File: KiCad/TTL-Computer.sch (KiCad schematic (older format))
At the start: 0 parts

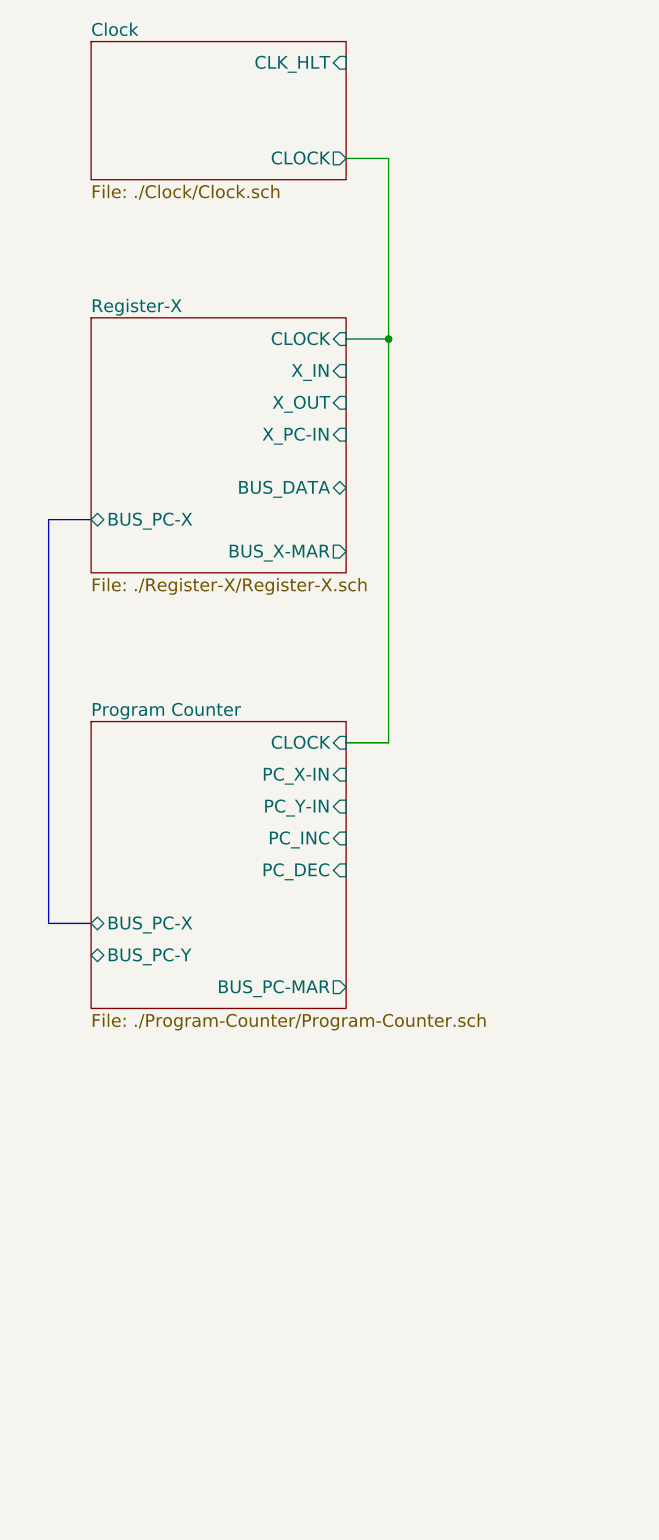
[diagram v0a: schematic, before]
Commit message: Started work on Program Counter
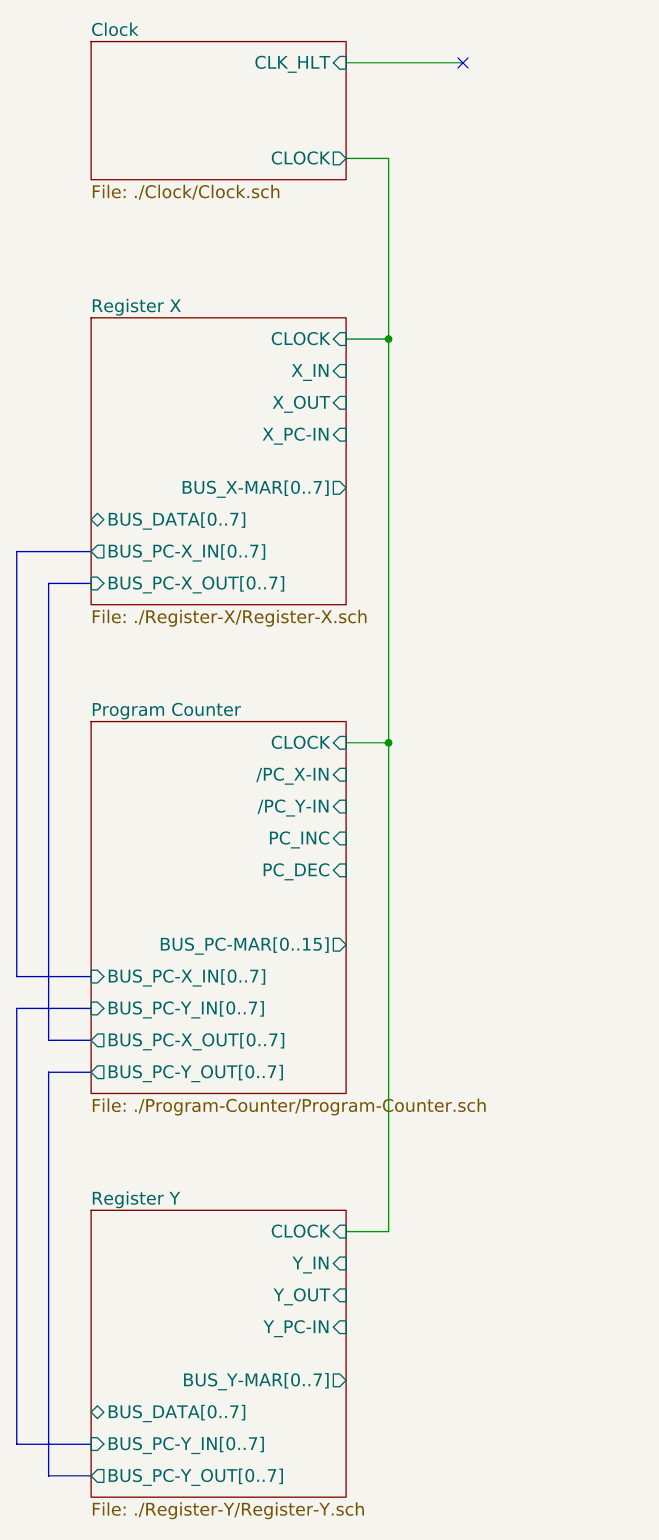
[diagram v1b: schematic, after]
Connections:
- no-connect marks 0 -> 1
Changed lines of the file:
@@
 EESchema Schematic File Version 2
+LIBS:TTL-Computer-rescue
 LIBS:power
 LIBS:device
@@
 EELAYER 25 0
 EELAYER END
-$Descr A4 11693 8268
+$Descr A4 8268 11693 portrait
 encoding utf-8
-Sheet 1 4
+Sheet 1 5
 Title ""
 Date ""
@@
 $EndSheet
 $Sheet
-S 1100 4000 1200 1350
-U 5ACF340E
-F0 "Program Counter" 60
-F1 "./Program-Counter/Program-Counter.sch" 60
-F2 "PC_X-IN" I R 2300 4250 60
-F3 "PC_Y-IN" I R 2300 4400 60
-F4 "PC_INC" I R 2300 4550 60
-F5 "PC_DEC" I R 2300 4700 60
-F6 "CLOCK" I R 2300 4100 60
-F7 "BUS_PC-X" B L 1100 4950 60
-F8 "BUS_PC-Y" B L 1100 5100 60
-F9 "BUS_PC-MAR" O R 2300 5250 60
-$EndSheet
-$Sheet
-S 1100 2100 1200 1200
+S 1100 2100 1200 1350
 U 5ACF2F0F
-F0 "Register-X" 60
+F0 "Register X" 60
 F1 "./Register-X/Register-X.sch" 60
 F2 "CLOCK" I R 2300 2200 60
@@
 F4 "X_OUT" I R 2300 2500 60
 F5 "X_PC-IN" I R 2300 2650 60
-F6 "BUS_DATA" B R 2300 2900 60
-F7 "BUS_PC-X" B L 1100 3050 60
-F8 "BUS_X-MAR" O R 2300 3200 60
+F6 "BUS_DATA[0..7]" B L 1100 3050 60
+F7 "BUS_PC-X_OUT[0..7]" I L 1100 3350 60
+F8 "BUS_X-MAR[0..7]" O R 2300 2900 60
+F9 "BUS_PC-X_IN[0..7]" O L 1100 3200 60
 $EndSheet
 Wire Bus Line
-	1100 3050 900  3050
+	1100 3350 900  3350
 Wire Bus Line
-	900  3050 900  4950
+	900  3350 900  5500
 Wire Bus Line
-	900  4950 1100 4950
+	900  5500 1100 5500
 Wire Wire Line
 	2300 1350 2500 1350
 Wire Wire Line
-	2500 1350 2500 4100
+	2500 1350 2500 6400
 Wire Wire Line
 	2500 2200 2300 2200
@@
 	2500 4100 2300 4100
 Connection ~ 2500 2200
+Wire Bus Line
+	1100 3200 750  3200
+Wire Bus Line
+	750  3200 750  5200
+Wire Bus Line
+	750  5200 1100 5200
+NoConn ~ 2850 900
+Wire Wire Line
+	2850 900  2300 900
+$Sheet
+S 1100 6300 1200 1350
+U 5AD0848F
+F0 "Register Y" 60
+F1 "./Register-Y/Register-Y.sch" 60
+F2 "BUS_PC-Y_IN[0..7]" I L 1100 7400 60
+F3 "BUS_DATA[0..7]" B L 1100 7250 60
+F4 "CLOCK" I R 2300 6400 60
+F5 "BUS_Y-MAR[0..7]" O R 2300 7100 60
+F6 "Y_IN" I R 2300 6550 60
+F7 "Y_OUT" I R 2300 6700 60
+F8 "Y_PC-IN" I R 2300 6850 60
+F9 "BUS_PC-Y_OUT[0..7]" O L 1100 7550 60
+$EndSheet
+Wire Bus Line
+	1100 5350 750  5350
+Wire Bus Line
+	750  5350 750  7400
+Wire Bus Line
+	750  7400 1100 7400
+Wire Bus Line
+	1100 5650 900  5650
+Wire Bus Line
+	900  5650 900  7550
+Wire Bus Line
+	900  7550 1100 7550
+$Sheet
+S 1100 4000 1200 1750
+U 5ACF340E
+F0 "Program Counter" 60
+F1 "./Program-Counter/Program-Counter.sch" 60
+F2 "/PC_X-IN" I R 2300 4250 60
+F3 "/PC_Y-IN" I R 2300 4400 60
+F4 "PC_INC" I R 2300 4550 60
+F5 "PC_DEC" I R 2300 4700 60
+F6 "CLOCK" I R 2300 4100 60
+F7 "BUS_PC-X_OUT[0..7]" O L 1100 5500 60
+F8 "BUS_PC-Y_OUT[0..7]" O L 1100 5650 60
+F9 "BUS_PC-MAR[0..15]" O R 2300 5050 60
+F10 "BUS_PC-X_IN[0..7]" I L 1100 5200 60
+F11 "BUS_PC-Y_IN[0..7]" I L 1100 5350 60
+$EndSheet
+Wire Wire Line
+	2500 6400 2300 6400
+Connection ~ 2500 4100
 $EndSCHEMATC

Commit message: Just more work in progress...
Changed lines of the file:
@@
 F1 "./Register-X/Register-X.sch" 60
 F2 "CLOCK" I R 2300 2200 60
-F3 "X_IN" I R 2300 2350 60
-F4 "X_OUT" I R 2300 2500 60
-F5 "X_PC-IN" I R 2300 2650 60
+F3 "/X_IN" I R 2300 2350 60
+F4 "/X_OUT" I R 2300 2500 60
+F5 "/X_PC-IN" I R 2300 2650 60
 F6 "BUS_DATA[0..7]" B L 1100 3050 60
 F7 "BUS_PC-X_OUT[0..7]" I L 1100 3350 60
@@
 F4 "CLOCK" I R 2300 6400 60
 F5 "BUS_Y-MAR[0..7]" O R 2300 7100 60
-F6 "Y_IN" I R 2300 6550 60
-F7 "Y_OUT" I R 2300 6700 60
-F8 "Y_PC-IN" I R 2300 6850 60
+F6 "/Y_IN" I R 2300 6550 60
+F7 "/Y_OUT" I R 2300 6700 60
+F8 "/Y_PC-IN" I R 2300 6850 60
 F9 "BUS_PC-Y_OUT[0..7]" O L 1100 7550 60
 $EndSheet
